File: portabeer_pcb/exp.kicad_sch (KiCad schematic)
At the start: 13 parts, among them J4 I2C expansion, U12 PCA9536DP, U13 GBI7254MMAR, U16 MCP47FEB12, U17 REF3012

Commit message: working
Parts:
- C16: now not fitted
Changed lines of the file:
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@@
 		(exclude_from_sim no)
 		(in_bom yes)
-		(on_board yes)
-		(dnp no)
+		(on_board no)
+		(dnp yes)
 		(fields_autoplaced yes)
 		(property "Reference" "C16"

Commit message: partial routing
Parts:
- removed J4: I2C expansion, Connector_PinHeader_2.54mm:PinHeader_1x05_P2.54mm_Vertical, symbol Connector_Generic:Conn_01x05
- removed U13: GBI7254MMAR, Package_SO:MSOP-8-1EP_3x3mm_P0.65mm_EP1.95x2.15mm, symbol Driver_FET:PM8834M
- added C54: 10u, Capacitor_SMD:C_1206_3216Metric, symbol Device:C
- added C60: 1u, Capacitor_SMD:C_0603_1608Metric, symbol Device:C
- added C65: C, Capacitor_SMD:C_0603_1608Metric, symbol Device:C
- added C67: 1n, Capacitor_SMD:C_0603_1608Metric, symbol Device:C
- added D9: PMEG3030EP, Diode_SMD:D_SOD-128, symbol Device:D_Schottky
- added J16: Conn_01x03, Connector_JST:JST_XH_B3B-XH-A_1x03_P2.50mm_Vertical, symbol Connector_Generic:Conn_01x03
- added J4: Conn_01x08, Connector_PinHeader_2.54mm:PinHeader_1x08_P2.54mm_Vertical, symbol Connector_Generic:Conn_01x08
- added JP11: SolderJumper_2_Open, Jumper:SolderJumper-2_P1.3mm_Open_RoundedPad1.0x1.5mm, symbol Jumper:SolderJumper_2_Open
- added JP7: SolderJumper_3_Open, Jumper:SolderJumper-3_P1.3mm_Open_RoundedPad1.0x1.5mm, symbol Jumper:SolderJumper_3_Open
- added M1: Air pump, Connector_Phoenix_MC:PhoenixContact_MC_1,5_2-G-3.81_1x02_P3.81mm_Horizontal, symbol Connector:Screw_Terminal_01x02
- added Q6: SiS454DN, portabeer:Vishay_PowerPAK_1212-8_Single, symbol Transistor_FET:SiS454DN
- added R60: 10, Resistor_SMD:R_0603_1608Metric, symbol Device:R
- added R61: 1k, Resistor_SMD:R_0603_1608Metric, symbol Device:R
- added R62: 1.96k, Resistor_SMD:R_0603_1608Metric, symbol Device:R
- added U4: COS1416, Package_TO_SOT_SMD:SOT-23-5, symbol Driver_FET:MCP1416
- R58: value 100 -> 10k
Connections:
- net AP_EN_2 is gone; now on net AP_EN: R58.1
- net +3.3V: now also J4.7 (Pin_7), JP7.1 (A)
- net +5V: now also J4.8 (Pin_8), JP7.3 (B)
- net GND: now also R58.2, C54.2, C60.2, C65.2, C67.2, J16.1 (Pin_1), J4.1 (Pin_1), JP11.1 (A), Q6.1 (S), Q6.2 (S), Q6.3 (S), U4.4 (GND)
- net SCL: now also J4.3 (Pin_3)
- net SDA: now also J4.2 (Pin_2)
- net VCC: now also C54.1, C60.1, D9.1 (K), M1.2 (Pin_2), U4.2 (Vdd)
- net at R54.2: now also U4.3 (IN)
- net AP_EN_1 renamed AP_EN
- new net: JP11.2 (B), R62.1
- new net: R60.1, U4.5 (OUT)
- new net: J16.2 (Pin_2), R61.2
- new net: Q6.4 (G), R60.2
- new net AP: D9.2 (A), M1.1 (Pin_1), Q6.5 (D)
- new net IO20: J4.6 (Pin_6)
- new net IO25: J4.5 (Pin_5)
- new net IO29: J4.4 (Pin_4)
- new net PRESS: C67.1, R61.1, R62.2
- new net VCC_PRESS: C65.1, J16.3 (Pin_3), JP7.2 (C)
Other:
- moved on the sheet: C108, C16, C63, C83, C86, R54, R58, R59, U12, U16, U17

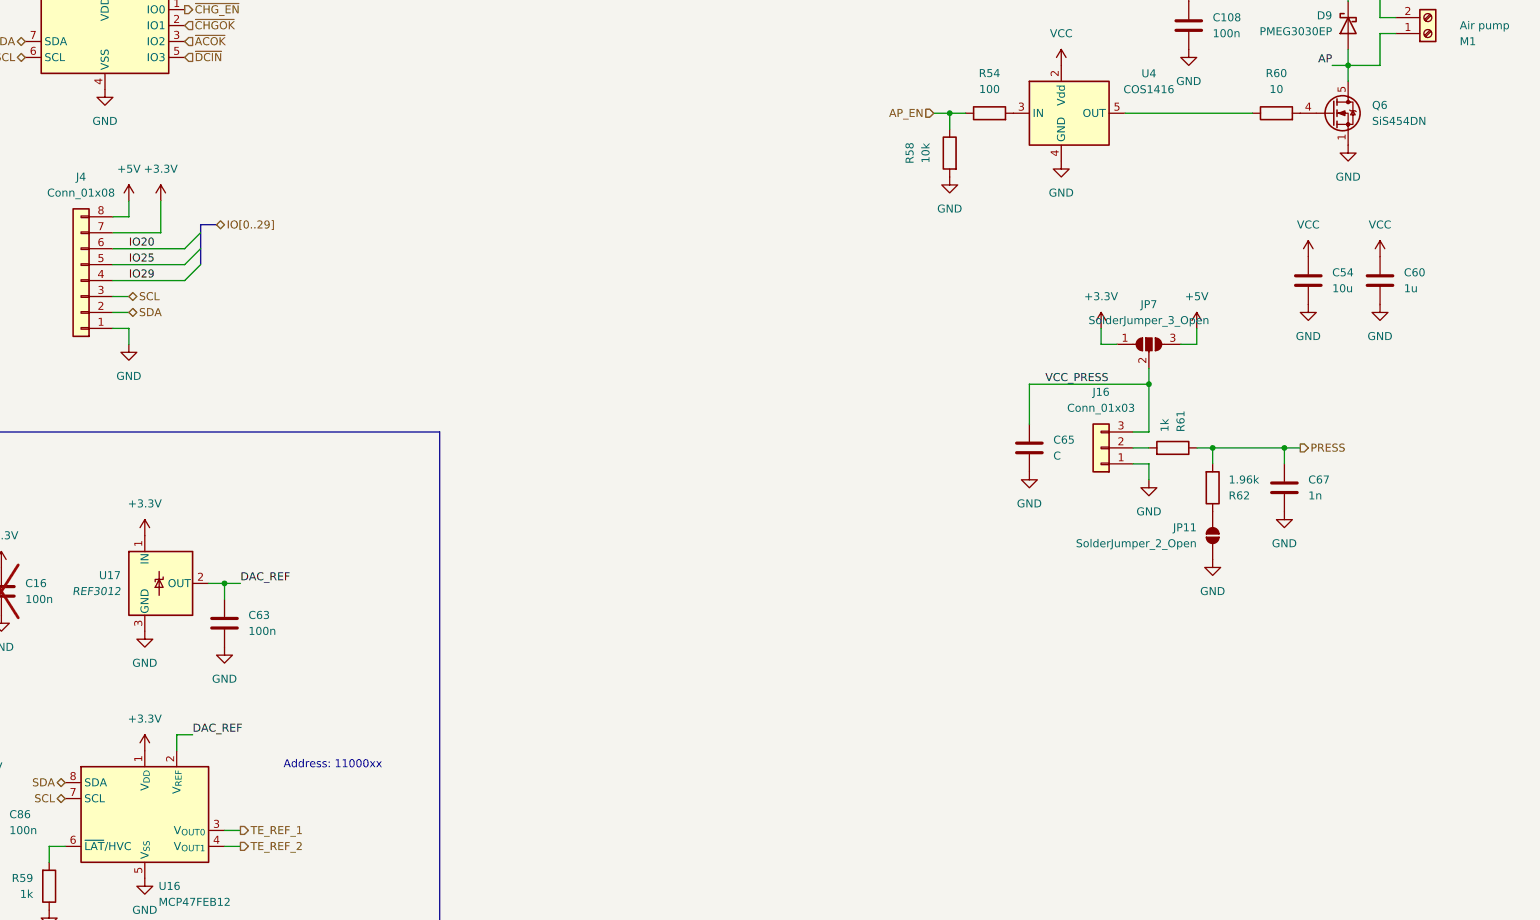
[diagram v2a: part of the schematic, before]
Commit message: added capacitive sensor
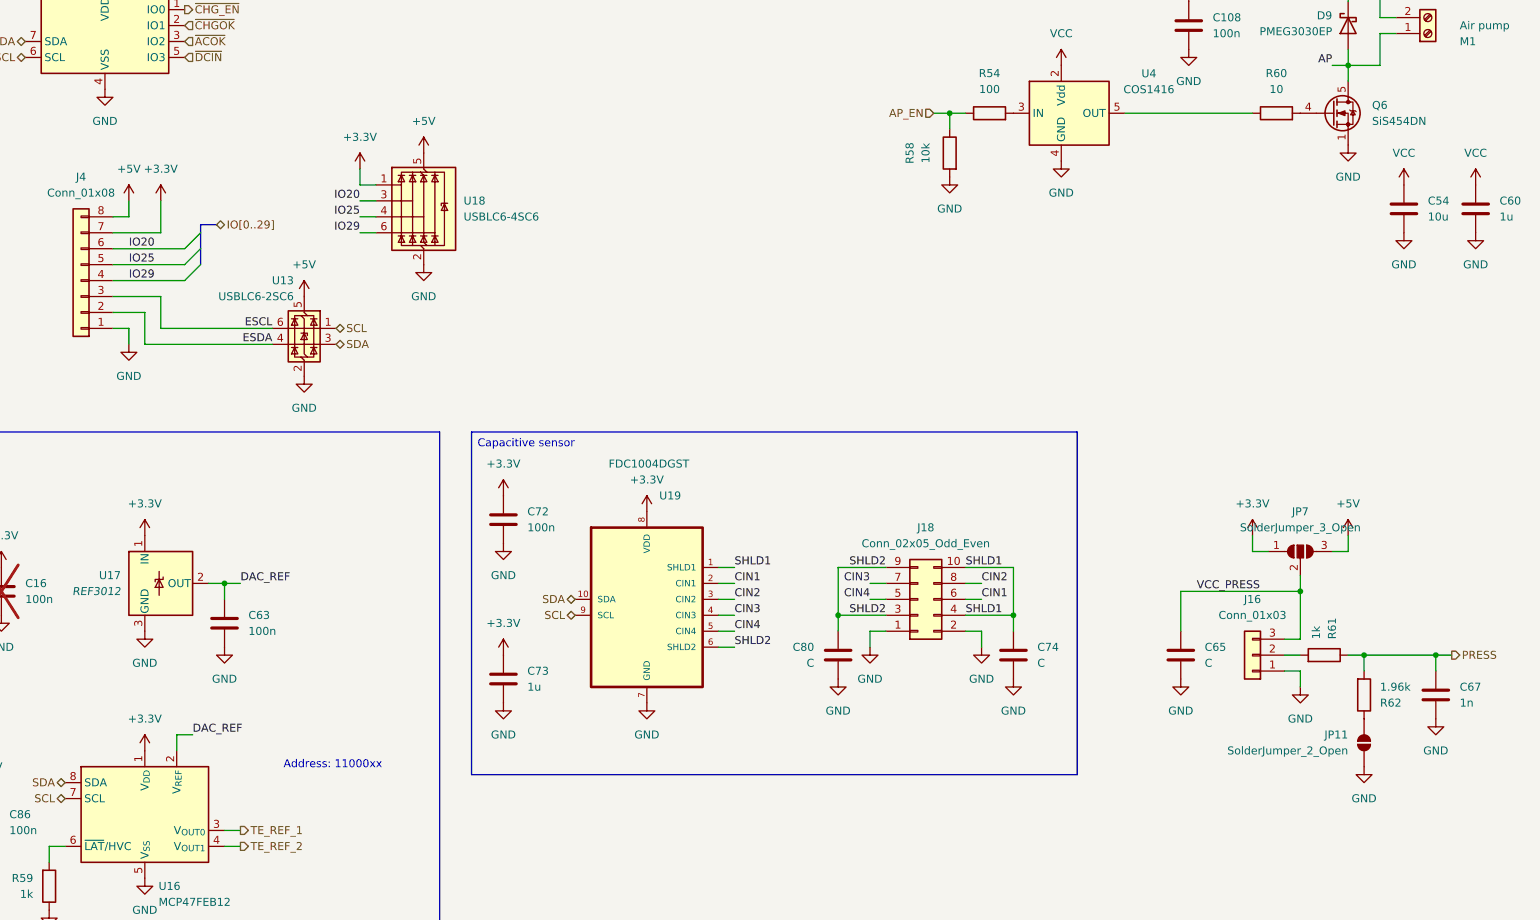
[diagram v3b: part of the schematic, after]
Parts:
- added C72: 100n, Capacitor_SMD:C_0603_1608Metric, symbol Device:C
- added C73: 1u, Capacitor_SMD:C_0603_1608Metric, symbol Device:C
- added C74, C80: C, Capacitor_SMD:C_0603_1608Metric, symbol Device:C
- added J18: Conn_02x05_Odd_Even, Connector_PinHeader_2.54mm:PinHeader_2x05_P2.54mm_Vertical, symbol Connector_Generic:Conn_02x05_Odd_Even
- added U13: USBLC6-2SC6, Package_TO_SOT_SMD:SOT-23-6, symbol Power_Protection:USBLC6-2SC6
- added U18: USBLC6-4SC6, Package_TO_SOT_SMD:SOT-23-6, symbol Power_Protection:USBLC6-4SC6
- added U19: FDC1004DGST, Package_SO:VSSOP-10_3x3mm_P0.5mm, symbol portabeer:FDC1004DGST
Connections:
- net +3.3V: now also C72.1, C73.1, U18.1 (I/O1), U19.8 (VDD)
- net +5V: now also U13.5 (VBUS), U18.5 (VBUS)
- net GND: now also C72.2, C73.2, C74.2, C80.2, J18.1 (Pin_1), J18.2 (Pin_2), U13.2 (GND), U18.2 (GND), U19.7 (GND)
- net IO20: now also U18.3 (I/O2)
- net IO25: now also U18.4 (I/O3)
- net IO29: now also U18.6 (I/O4)
- net SCL: now also U13.1 (I/O1), U19.9 (SCL); no longer J4.3 (Pin_3)
- net SDA: now also U13.3 (I/O2), U19.10 (SDA); no longer J4.2 (Pin_2)
- new net CIN1: J18.6 (Pin_6), U19.2 (CIN1)
- new net CIN2: J18.8 (Pin_8), U19.3 (CIN2)
- new net CIN3: J18.7 (Pin_7), U19.4 (CIN3)
- new net CIN4: J18.5 (Pin_5), U19.5 (CIN4)
- new net ESCL: J4.3 (Pin_3), U13.6 (I/O1)
- new net ESDA: J4.2 (Pin_2), U13.4 (I/O2)
- new net SHLD1: C74.1, J18.10 (Pin_10), J18.4 (Pin_4), U19.1 (SHLD1)
- new net SHLD2: C80.1, J18.3 (Pin_3), J18.9 (Pin_9), U19.6 (SHLD2)
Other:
- moved on the sheet: C54, C60, C65, C67, J16, JP11, JP7, R61, R62

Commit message: layout
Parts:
- removed J4: Conn_01x08, Connector_PinHeader_2.54mm:PinHeader_1x08_P2.54mm_Vertical, symbol Connector_Generic:Conn_01x08
- removed U18: USBLC6-4SC6, Package_TO_SOT_SMD:SOT-23-6, symbol Power_Protection:USBLC6-4SC6
- added C81, C82, C84: 100n, Capacitor_SMD:C_0603_1608Metric, symbol Device:C
- added D17: MBR0530, Diode_SMD:D_SOD-123, symbol Diode:MBR0530
- added J23: Conn_01x02, Connector_PinHeader_2.54mm:PinHeader_1x02_P2.54mm_Vertical, symbol Connector_Generic:Conn_01x02
- added J24, J25: Conn_01x04, Connector_PinHeader_2.54mm:PinHeader_1x04_P2.54mm_Vertical, symbol Connector_Generic:Conn_01x04
- added J4: Conn_01x02, Connector_JST:JST_XH_S2B-XH-A_1x02_P2.50mm_Horizontal, symbol Connector_Generic:Conn_01x02
- added Q9: AO3400A, Package_TO_SOT_SMD:SOT-23, symbol Transistor_FET:AO3400A
- added R71: 100k, Resistor_SMD:R_0603_1608Metric, symbol Device:R
- added R75: 10, Resistor_SMD:R_0603_1608Metric, symbol Device:R
- added U20: USBLC6-2SC6, Package_TO_SOT_SMD:SOT-23-6, symbol Power_Protection:USBLC6-2SC6
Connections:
- net +3.3V: now also U13.5 (VBUS), C81.1, C82.1, J24.4 (Pin_4), J25.4 (Pin_4), U20.5 (VBUS)
- net +5V: now also J23.2 (Pin_2); no longer U13.5 (VBUS)
- net ESCL: now also J24.3 (Pin_3)
- net ESDA: now also J24.2 (Pin_2)
- net GND: now also C81.2, C82.2, C84.2, J23.1 (Pin_1), J24.1 (Pin_1), J25.1 (Pin_1), Q9.2 (S), R71.1, U20.2 (GND)
- net VCC: now also C84.1, D17.1 (K), J4.1 (Pin_1)
- new net: Q9.1 (G), R75.2
- new net: J25.2 (Pin_2), U20.4 (I/O2)
- new net: J25.3 (Pin_3), U20.6 (I/O1)
- new net FAN: D17.2 (A), J4.2 (Pin_2), Q9.3 (D)
- new net FAN_EN: R71.2, R75.1
